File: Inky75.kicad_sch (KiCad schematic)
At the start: 176 parts, among them J1 J, K1 K, M1 M, P1 P, Q1 Q, T1 T, U1 KB2040, U2 U, X1 X, Y1 Y

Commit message: fixing traces
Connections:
- net Row_3: now also D46.1 (K)
- net at U2.2: now also D46.2 (A)
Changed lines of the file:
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@@
   (junction (at 236.22 83.82) (diameter 0) (color 0 0 0 0)
   )
+  (junction (at 236.22 91.44) (diameter 0) (color 0 0 0 0)
+  )
   (junction (at 217.17 147.32) (diameter 0) (color 0 0 0 0)
   )
@@
   (junction (at 102.87 68.58) (diameter 0) (color 0 0 0 0)
   )
+  (junction (at 236.22 99.06) (diameter 0) (color 0 0 0 0)
+  )
   (junction (at 293.37 91.44) (diameter 0) (color 0 0 0 0)
   )
@@
   (junction (at 293.37 132.08) (diameter 0) (color 0 0 0 0)
   )
-  (wire (pts (xy 217.17 99.06) (xy 255.27 99.06))
+  (wire (pts (xy 217.17 99.06) (xy 236.22 99.06))
     (stroke (width 0) (type default) (color 0 0 0 0))
   )
@@
     (stroke (width 0) (type default) (color 0 0 0 0))
   )
+  (wire (pts (xy 236.22 99.06) (xy 255.27 99.06))
+    (stroke (width 0) (type default) (color 0 0 0 0))
+  )
   (wire (pts (xy 347.98 76.2) (xy 350.52 76.2))
     (stroke (width 0) (type default) (color 0 0 0 0))
@@
     (pin "2")
   )
-  (symbol (lib_id "Diode:1N4148") (at 236.22 93.98 270) (mirror x) (unit 1)
+  (symbol (lib_id "Diode:1N4148") (at 236.22 95.25 270) (mirror x) (unit 1)
     (in_bom yes) (on_board yes)
-    (property "Reference" "D46" (id 0) (at 242.57 93.98 0)
+    (property "Reference" "D46" (id 0) (at 242.57 95.25 0)
       (effects (font (size 1.27 1.27)) hide)
     )
-    (property "Value" "1N4148" (id 1) (at 238.76 93.98 0))
-    (property "Footprint" "Diode_THT:D_DO-35_SOD27_P7.62mm_Horizontal" (id 2) (at 236.22 93.98 0)
+    (property "Value" "1N4148" (id 1) (at 238.76 95.25 0))
+    (property "Footprint" "Diode_THT:D_DO-35_SOD27_P7.62mm_Horizontal" (id 2) (at 236.22 95.25 0)
       (effects (font (size 1.27 1.27)) hide)
     )
-    (property "Datasheet" "https://assets.nexperia.com/documents/data-sheet/1N4148_1N4448.pdf" (id 3) (at 236.22 93.98 0)
+    (property "Datasheet" "https://assets.nexperia.com/documents/data-sheet/1N4148_1N4448.pdf" (id 3) (at 236.22 95.25 0)
       (effects (font (size 1.27 1.27)) hide)
     )

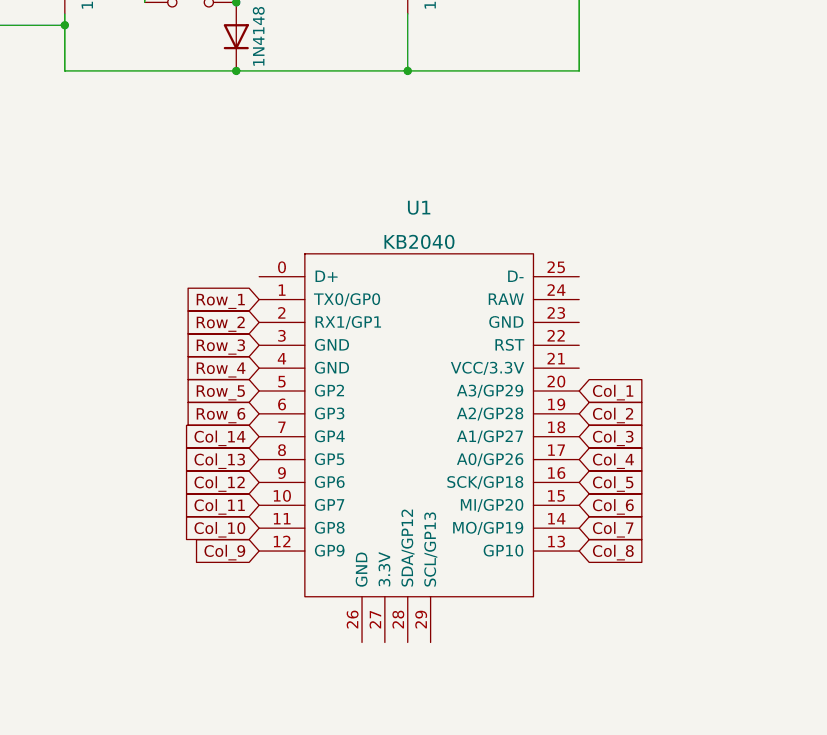
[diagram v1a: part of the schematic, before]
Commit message: finished routing traces
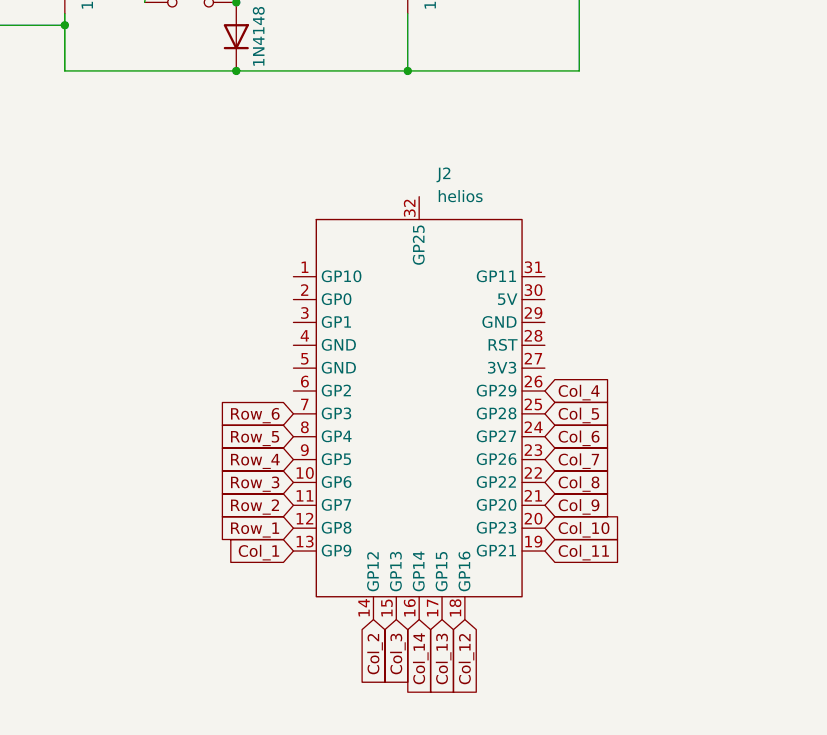
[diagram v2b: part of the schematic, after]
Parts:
- removed U1: KB2040, kb2040_NEW:KB2040_FINAAL, symbol kb2040:KB2040
- added J2: helios, 0xCB-HeliosFootprint:helios, symbol 0xcb:helios
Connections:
- net Col_1: now also J2.13 (GP9)
- net Col_10: now also J2.20 (GP23)
- net Col_11: now also J2.19 (GP21)
- net Col_12: now also J2.18 (GP16)
- net Col_13: now also J2.17 (GP15)
- net Col_14: now also J2.16 (GP14)
- net Col_2: now also J2.14 (GP12)
- net Col_3: now also J2.15 (GP13)
- net Col_4: now also J2.26 (GP29)
- net Col_5: now also J2.25 (GP28)
- net Col_6: now also J2.24 (GP27)
- net Col_7: now also J2.23 (GP26)
- net Col_8: now also J2.22 (GP22)
- net Col_9: now also J2.21 (GP20)
- net Row_1: now also J2.12 (GP8)
- net Row_2: now also J2.11 (GP7)
- net Row_3: now also J2.10 (GP6)
- net Row_4: now also J2.9 (GP5)
- net Row_5: now also J2.8 (GP4)
- net Row_6: now also J2.7 (GP3)

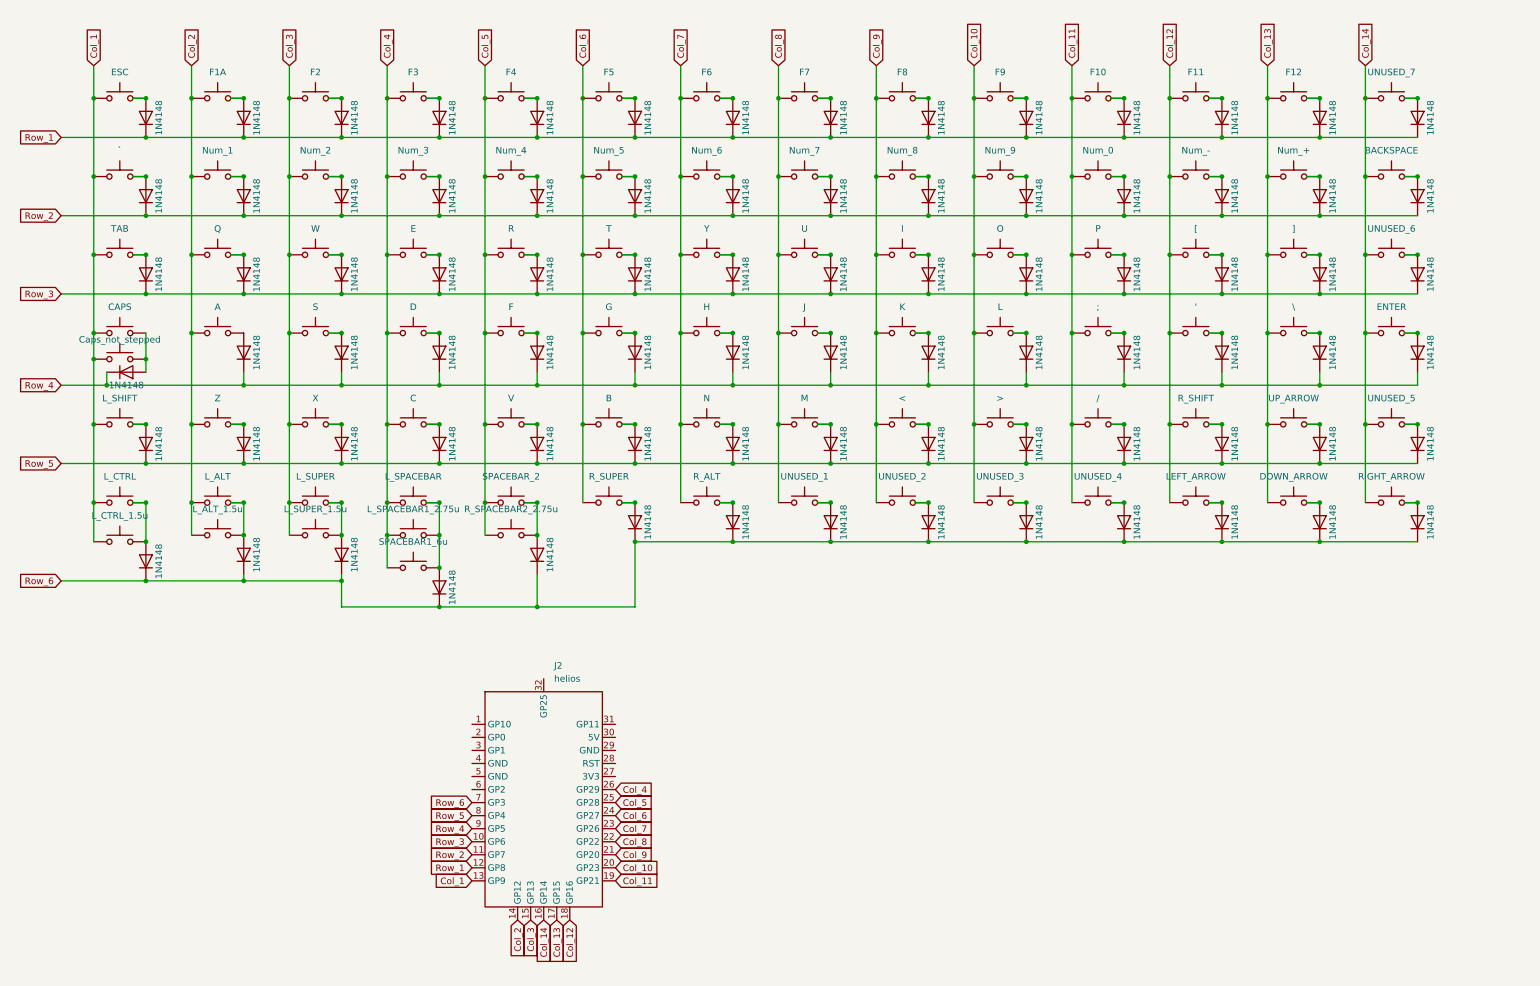
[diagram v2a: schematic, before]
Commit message: updated traces
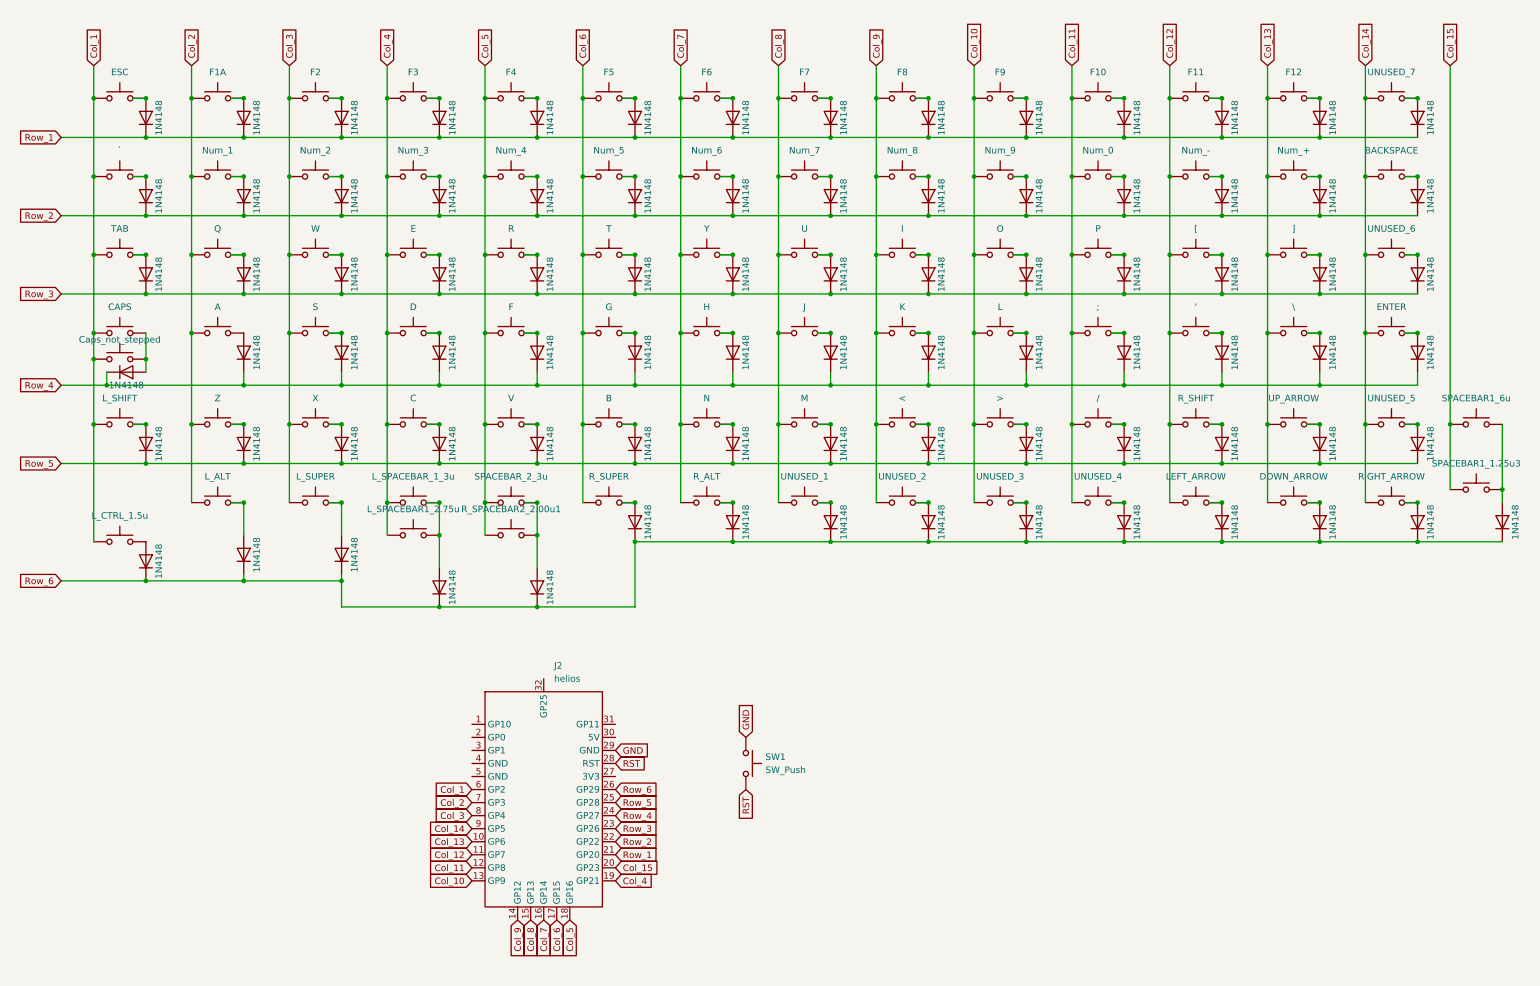
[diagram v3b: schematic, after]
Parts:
- removed L_ALT1.5u1: L_ALT_1.5u, Switch_Keyboard_Cherry_MX:SW_Cherry_MX_PCB_1.50u, symbol Switch:SW_Push
- removed L_CTRL1: L_CTRL, Switch_Keyboard_Cherry_MX:SW_Cherry_MX_PCB_1.25u, symbol Switch:SW_Push
- removed L_SUPER_1.5u1: L_SUPER_1.5u, Switch_Keyboard_Cherry_MX:SW_Cherry_MX_PCB_1.50u, symbol Switch:SW_Push
- added D86: 1N4148, Diode_THT:D_DO-35_SOD27_P7.62mm_Horizontal, symbol Diode:1N4148
- added SPACEBAR1_1.25u3: SPACEBAR1_1.25u3, Switch_Keyboard_Cherry_MX:SW_Cherry_MX_PCB_1.25u, symbol Switch:SW_Push
- added SW1: SW_Push, Button_Switch_SMD:SW_SPST_TL3342, symbol Switch:SW_Push
- J2: footprint 0xCB-HeliosFootprint:helios -> 0xCB-HeliosFootprint:helios_no-usb
- L_SPACEBAR1: value L_SPACEBAR -> L_SPACEBAR_1_3u
- R_SPACEBAR2_2.00u1: renamed from R_SPACEBAR2_2.75u1; value R_SPACEBAR2_2.75u -> R_SPACEBAR2_2.00u1; footprint Switch_Keyboard_Cherry_MX:SW_Cherry_MX_PCB_2.75u -> Switch_Keyboard_Cherry_MX:SW_Cherry_MX_PCB_2.00u
- SPACEBAR_2: value SPACEBAR_2 -> SPACEBAR_2_3u
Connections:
- net Col_1: now also J2.6 (GP2); no longer J2.13 (GP9)
- net Col_10: now also J2.13 (GP9); no longer J2.20 (GP23)
- net Col_11: now also J2.12 (GP8); no longer J2.19 (GP21)
- net Col_12: now also J2.11 (GP7); no longer J2.18 (GP16)
- net Col_13: now also J2.10 (GP6); no longer J2.17 (GP15)
- net Col_14: now also J2.9 (GP5); no longer J2.16 (GP14)
- net Col_2: now also J2.7 (GP3); no longer J2.14 (GP12)
- net Col_3: now also J2.8 (GP4); no longer J2.15 (GP13)
- net Col_4: now also J2.19 (GP21); no longer J2.26 (GP29), SPACEBAR1_6u1.1
- net Col_5: now also J2.18 (GP16); no longer J2.25 (GP28)
- net Col_6: now also J2.17 (GP15); no longer J2.24 (GP27)
- net Col_7: now also J2.16 (GP14); no longer J2.23 (GP26)
- net Col_8: now also J2.15 (GP13); no longer J2.22 (GP22)
- net Col_9: now also J2.14 (GP12); no longer J2.21 (GP20)
- net Row_1: now also J2.21 (GP20); no longer J2.12 (GP8)
- net Row_2: now also J2.22 (GP22); no longer J2.11 (GP7)
- net Row_3: now also J2.23 (GP26); no longer J2.10 (GP6)
- net Row_4: now also J2.24 (GP27); no longer J2.9 (GP5)
- net Row_5: now also J2.25 (GP28); no longer J2.8 (GP4)
- net Row_6: now also J2.26 (GP29), D86.1 (K); no longer J2.7 (GP3)
- net at D25.2 (A), L_SPACEBAR1.2, L_SPACEBAR1_2.75u1.2: no longer SPACEBAR1_6u1.2
- net RST: now reaches J2.28 (RST)
- net RST: now also SW1.2
- net GND: now reaches J2.29 (GND)
- net GND: now also SW1.1
- new net: D86.2 (A), SPACEBAR1_1.25u3.2, SPACEBAR1_6u1.2
- new net Col_15: J2.20 (GP23), SPACEBAR1_1.25u3.1, SPACEBAR1_6u1.1
